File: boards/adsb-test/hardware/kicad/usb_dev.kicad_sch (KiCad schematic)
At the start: 0 parts

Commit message: Release v0.22.0: all ADSB_Test schematic sheets generated (ERC clean)
Co-Authored-By: Claude Opus 5.5 <noreply@anthropic.com>
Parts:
- added C1001, C1003, C1004, C1022, C1023: 1uF, Capacitor_SMD:C_0805_2012Metric_Pad1.18x1.45mm_HandSolder, symbol Device:C
- added C1002: 10uF, Capacitor_SMD:C_1206_3216Metric_Pad1.33x1.80mm_HandSolder, symbol Device:C
- added C1005, C1008, C1009, C1010, C1011, C1013, C1014, C1015, C1016, C1024, C1025, C1026, C1027, C1028, C1029, C1030, C1031, C1032, C1033, C1034, C1035, C1036, C1037: 100nF, Capacitor_SMD:C_0805_2012Metric_Pad1.18x1.45mm_HandSolder, symbol Device:C
- added C1006, C1007: 18pF, Capacitor_SMD:C_0805_2012Metric_Pad1.18x1.45mm_HandSolder, symbol Device:C
- added C1012, C1017: 4.7uF, Capacitor_SMD:C_0805_2012Metric_Pad1.18x1.45mm_HandSolder, symbol Device:C
- added C1018, C1019: 27pF, Capacitor_SMD:C_0805_2012Metric_Pad1.18x1.45mm_HandSolder, symbol Device:C
- added C1020, C1021: 15pF, Capacitor_SMD:C_0805_2012Metric_Pad1.18x1.45mm_HandSolder, symbol Device:C
- added D1001: 1N4148W, Diode_SMD:D_SOD-123, symbol Device:D
- added D1002: WS2812B, LED_SMD:LED_WS2812B_PLCC4_5.0x5.0mm_P3.2mm, symbol LED:WS2812B
- added J1001: Dev USB-C, Connector_USB:USB_C_Receptacle_GCT_USB4105-xx-A_16P_TopMnt_Horizontal, symbol Connector:USB_C_Receptacle_USB2.0_16P
- added Q1001, Q1002, Q1003, Q1004: MMBT3904, Package_TO_SOT_SMD:SOT-23_Handsoldering, symbol Transistor_BJT:MMBT3904
- added R1001, R1002: 5.1k, Resistor_SMD:R_0805_2012Metric_Pad1.20x1.40mm_HandSolder, symbol Device:R
- added R1003, R1004, R1005, R1006, R1007, R1008, R1010, R1015, R1017, R1018, R1019, R1020, R1021, R1022, R1023, R1024, R1025, R1033, R1034, R1039: 10k, Resistor_SMD:R_0805_2012Metric_Pad1.20x1.40mm_HandSolder, symbol Device:R
- added R1009, R1014: 12k 1%, Resistor_SMD:R_0805_2012Metric_Pad1.20x1.40mm_HandSolder, symbol Device:R
- added R1011, R1012, R1040: 100k, Resistor_SMD:R_0805_2012Metric_Pad1.20x1.40mm_HandSolder, symbol Device:R
- added R1013: 1M, Resistor_SMD:R_0805_2012Metric_Pad1.20x1.40mm_HandSolder, symbol Device:R
- added R1016: 2.2k, Resistor_SMD:R_0805_2012Metric_Pad1.20x1.40mm_HandSolder, symbol Device:R
- added R1030, R1031: 27R, Resistor_SMD:R_0805_2012Metric_Pad1.20x1.40mm_HandSolder, symbol Device:R
- added R1032, R1035: 1k, Resistor_SMD:R_0805_2012Metric_Pad1.20x1.40mm_HandSolder, symbol Device:R
- added R1036: 330R, Resistor_SMD:R_0805_2012Metric_Pad1.20x1.40mm_HandSolder, symbol Device:R
- added R1037, R1038: 0R, Resistor_SMD:R_0805_2012Metric_Pad1.20x1.40mm_HandSolder, symbol Device:R
- added SW1001: BOOTSEL (programmer), Button_Switch_THT:SW_PUSH_6mm, symbol Switch:SW_Push
- added TP1001: VBUS_DEV, TestPoint:TestPoint_Pad_D1.5mm, symbol Connector:TestPoint
- added TP1002: 3V3_DEV, TestPoint:TestPoint_Pad_D1.5mm, symbol Connector:TestPoint
- added TP1003: RP_SWCLK, TestPoint:TestPoint_Pad_D1.5mm, symbol Connector:TestPoint
- added TP1004: RP_SWDIO, TestPoint:TestPoint_Pad_D1.5mm, symbol Connector:TestPoint
- added TP1005: RP_RUN, TestPoint:TestPoint_Pad_D1.5mm, symbol Connector:TestPoint
- added TP1006: FT_A_DTR, TestPoint:TestPoint_Pad_D1.5mm, symbol Connector:TestPoint
- added TP1007: FT_A_RTS, TestPoint:TestPoint_Pad_D1.5mm, symbol Connector:TestPoint
- added TP1008: FT_B_DTR, TestPoint:TestPoint_Pad_D1.5mm, symbol Connector:TestPoint
- added TP1009: FT_B_RTS, TestPoint:TestPoint_Pad_D1.5mm, symbol Connector:TestPoint
- added U1001: USBLC6-2SC6, Package_TO_SOT_SMD:SOT-23-6_Handsoldering, symbol Power_Protection:USBLC6-2SC6
- added U1002: AP2112K-3.3, Package_TO_SOT_SMD:SOT-23-5_HandSoldering, symbol Regulator_Linear:AP2112K-3.3
- added U1003: USB2514B, ADSB_Test:QFN-36-1EP_6x6mm_P0.5mm_EP3.7x3.7mm_HandSolder, symbol Interface_USB:USB2514B_Bi
- added U1004: FT2232HL, Package_QFP:LQFP-64_10x10mm_P0.5mm, symbol Interface_USB:FT2232HL
- added U1005: 93LC56B, Package_SO:SOIC-8_3.9x4.9mm_P1.27mm, symbol Memory_EEPROM:93LCxxB
- added U1006, U1008: 74LVC1G07, Package_TO_SOT_SMD:SOT-23-5_HandSoldering, symbol 74xGxx:74LVC1G07
- added U1007, U1009, U1012, U1013, U1014, U1015: 74LVC1G125, Package_TO_SOT_SMD:SOT-23-5_HandSoldering, symbol 74xGxx:74LVC1G125
- added U1010: RP2040, ADSB_Test:QFN-56-1EP_7x7mm_P0.4mm_EP3.2x3.2mm_HandSolder, symbol MCU_RaspberryPi:RP2040
- added U1011: W25Q16JVSS, Package_SO:SOIC-8_5.3x5.3mm_P1.27mm, symbol Memory_Flash:W25Q16JVSS
- added Y1001: 24MHz, Crystal:Crystal_SMD_5032-2Pin_5.0x3.2mm_HandSoldering, symbol Device:Crystal
- added Y1002, Y1003: 12MHz, Crystal:Crystal_SMD_5032-2Pin_5.0x3.2mm_HandSoldering, symbol Device:Crystal
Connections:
- new net 3V3: R1020.1, R1021.1
- new net 3V3_DEV: C1002.1, C1008.1, C1009.1, C1010.1, C1011.1, C1012.1, C1015.1, C1016.1, C1022.1, C1024.1, C1025.1, C1026.1, C1028.1, C1030.1, C1031.1, C1032.1, C1033.1, C1034.1, C1035.1, C1036.1, C1037.1, R1003.1, R1004.1, R1010.1, R1015.1, R1017.1, R1018.1, R1019.1, R1033.1, R1034.1, R1039.1, TP1002.1, U1002.5 (VOUT), U1003.10 (VDDA33), U1003.15 (VDD33), U1003.23 (VDD33), U1003.29 (VDDA33), U1003.36 (VDDA33), U1003.5 (VDDA33), U1004.20 (VCCIO), U1004.31 (VCCIO), U1004.4 (VPHY), U1004.42 (VCCIO), U1004.50 (VREGIN), U1004.56 (VCCIO), U1004.9 (VPLL), U1005.8 (VCC), U1006.5 (VCC), U1007.5 (VCC), U1008.5 (VCC), U1009.5 (VCC), U1010.1 (IOVDD), U1010.10 (IOVDD), U1010.22 (IOVDD), U1010.33 (IOVDD), U1010.42 (IOVDD), U1010.43 (ADC_AVDD), U1010.44 (VREG_VIN), U1010.48 (USB_VDD), U1010.49 (IOVDD), U1011.8 (VCC), U1012.5 (VCC), U1013.5 (VCC), U1014.5 (VCC), U1015.5 (VCC)
- new net C5_BOOT: Q1004.3 (C)
- new net C5_CON_RX: R1021.2, U1008.4
- new net C5_CON_TX: U1009.2
- new net C5_EN: Q1003.3 (C)
- new net DEV_CC1: J1001.A5 (CC1), R1001.1
- new net DEV_CC2: J1001.B5 (CC2), R1002.1
- new net DEV_DM: J1001.A7 (D-), J1001.B7 (D-), U1001.3 (I/O2), U1001.4 (I/O2), U1003.30 (USBDM_UP)
- new net DEV_DP: J1001.A6 (D+), J1001.B6 (D+), U1001.1 (I/O1), U1001.6 (I/O1), U1003.31 (USBDP_UP)
- new net DEV_M1421_NRST: U1012.4
- new net DEV_M1421_SYNC: U1013.4
- new net DEV_M1421_TX: U1014.4
- new net ETH_TXD1_BOOT: Q1002.3 (C)
- new net FT_1V8: C1013.1, C1014.1, C1017.1, U1004.12 (VCORE), U1004.37 (VCORE), U1004.49 (VREGOUT), U1004.64 (VCORE)
- new net FT_A_DTR: Q1002.2 (E), R1022.1, TP1006.1, U1004.21 (ADBUS4)
- new net FT_A_RTS: Q1001.2 (E), R1023.1, TP1007.1, U1004.18 (ADBUS2)
- new net FT_A_RXD: U1004.17 (ADBUS1), U1007.4
- new net FT_A_TXD: U1004.16 (ADBUS0), U1006.2
- new net FT_B_DTR: Q1004.2 (E), R1024.1, TP1008.1, U1004.43 (BDBUS4)
- new net FT_B_RTS: Q1003.2 (E), R1025.1, TP1009.1, U1004.40 (BDBUS2)
- new net FT_B_RXD: U1004.39 (BDBUS1), U1009.4
- new net FT_B_TXD: U1004.38 (BDBUS0), U1008.2
- new net FT_DM: U1003.6 (USBDM_DN3/PRT_DIS_M3), U1004.7 (DM)
- new net FT_DP: U1003.7 (USBDP_DN3/PRT_DIS_P3), U1004.8 (DP)
- new net FT_EECLK: R1018.2, U1004.62 (EECLK), U1005.2 (SCLK)
- new net FT_EECS: R1017.2, U1004.63 (EECS), U1005.1 (CS)
- new net FT_EEDATA: R1016.2, R1019.2, U1004.61 (EEDATA), U1005.3 (DI)
- new net FT_EEDO: R1016.1, U1005.4 (DO)
- new net FT_REF: R1014.1, U1004.6 (REF)
- new net FT_RESET: R1015.2, U1004.14 (~{RESET})
- new net FT_XI: C1018.1, U1004.2 (OSCI), Y1002.1
- new net FT_XO: C1019.1, U1004.3 (OSCO), Y1002.2
- new net GND: C1001.2, C1002.2, C1003.2, C1004.2, C1005.2, C1006.2, C1007.2, C1008.2, C1009.2, C1010.2, C1011.2, C1012.2, C1013.2, C1014.2, C1015.2, C1016.2, C1017.2, C1018.2, C1019.2, C1020.2, C1021.2, C1022.2, C1023.2, C1024.2, C1025.2, C1026.2, C1027.2, C1028.2, C1029.2, C1030.2, C1031.2, C1032.2, C1033.2, C1034.2, C1035.2, C1036.2, C1037.2, D1002.3 (VSS), J1001.A1 (GND), J1001.A12 (GND), J1001.B1 (GND), J1001.B12 (GND), J1001.SH (SHIELD), R1001.2, R1002.2, R1005.2, R1006.2, R1007.2, R1008.2, R1009.2, R1012.2, R1014.2, R1040.2, SW1001.2, U1001.2 (GND), U1002.2 (GND), U1003.11 (TEST), U1003.37 (VSS), U1004.1 (GND), U1004.10 (AGND), U1004.11 (GND), U1004.13 (TEST), U1004.15 (GND), U1004.25 (GND), U1004.35 (GND), U1004.47 (GND), U1004.5 (GND), U1004.51 (GND), U1005.5 (GND), U1006.3 (GND), U1007.1, U1007.3 (GND), U1008.3 (GND), U1009.1, U1009.3 (GND), U1010.19 (TESTEN), U1010.57 (GND), U1011.4 (GND), U1012.1, U1012.3 (GND), U1013.1, U1013.3 (GND), U1014.1, U1014.3 (GND), U1015.1, U1015.3 (GND)
- new net HUB_CFG0: R1005.1, U1003.24 (SCL/SMBCLK/CFG_SEL0)
- new net HUB_CFG1: R1006.1, U1003.25 (HS_IND/CFG_SEL1)
- new net HUB_CRFILT: C1003.1, U1003.14 (CRFILT)
- new net HUB_DN2_M: R1004.2, U1003.3 (USBDM_DN2/PRT_DIS_M2)
- new net HUB_DN2_P: R1003.2, U1003.4 (USBDP_DN2/PRT_DIS_P2)
- new net HUB_NONREM0: R1007.1, U1003.28 (SUSP_IND/LOCAL_PWR/NON_REM0)
- new net HUB_NONREM1: R1008.1, U1003.22 (SDA/SMBDATA/NON_REM1)
- new net HUB_PLLFILT: C1004.1, U1003.34 (PLLFILT)
- new net HUB_RBIAS: R1009.1, U1003.35 (RBIAS)
- new net HUB_RESET: C1005.1, R1010.2, U1003.26 (RESET_N)
- new net HUB_VBUS_DET: R1011.2, R1012.1, U1003.27 (VBUS_DET)
- new net HUB_XI: C1006.1, R1013.1, U1003.33 (XTALIN/CLKIN), Y1001.1
- new net HUB_XO: C1007.1, R1013.2, U1003.32 (XTALOUT), Y1001.2
- new net LED_VDD: C1029.1, D1001.1 (K), D1002.1 (VDD)
- new net M1421_SUTX: U1015.2
- new net P4_CON_RX: R1020.2, U1006.4
- new net P4_CON_TX: U1007.2
- new net P4_EN: Q1001.3 (C)
- new net P4_USJ_DM: U1003.1 (USBDM_DN1/PRT_DIS_M1)
- new net P4_USJ_DP: U1003.2 (USBDP_DN1/PRT_DIS_P1)
- new net QA1_B: Q1001.1 (B), R1022.2
- new net QA2_B: Q1002.1 (B), R1023.2
- new net QB1_B: Q1003.1 (B), R1024.2
- new net QB2_B: Q1004.1 (B), R1025.2
- new net RP_1V1: C1023.1, C1027.1, U1010.23 (DVDD), U1010.45 (VREG_VOUT), U1010.50 (DVDD)
- new net RP_BOOTSEL: R1035.2, SW1001.1
- new net RP_DM: R1031.2, U1010.46 (USB_DM)
- new net RP_DM_H: R1031.1, U1003.8 (USBDM_DN4/PRT_DIS_M4)
- new net RP_DP: R1030.2, U1010.47 (USB_DP)
- new net RP_DP_H: R1030.1, U1003.9 (USBDP_DN4/PRT_DIS_P4)
- new net RP_LED: R1036.1, U1010.27 (GPIO16)
- new net RP_LED_D: D1002.4 (DIN), R1036.2
- new net RP_NRST: R1037.1, U1010.38 (GPIO26/ADC0)
- new net RP_NRST_L: R1037.2, R1039.2, U1012.2
- new net RP_QD0: U1010.53 (QSPI_SD0), U1011.5 (DI/IO_{0})
- new net RP_QD1: U1010.55 (QSPI_SD1), U1011.2 (DO/IO_{1})
- new net RP_QD2: U1010.54 (QSPI_SD2), U1011.3 (~{WP}/IO_{2})
- new net RP_QD3: U1010.51 (QSPI_SD3), U1011.7 (~{HOLD}/~{RESET}/IO_{3})
- new net RP_QSCK: U1010.52 (QSPI_SCLK), U1011.6 (CLK)
- new net RP_QSS: R1034.2, R1035.1, U1010.56 (~{QSPI_SS}), U1011.1 (~{CS})
- new net RP_RUN: R1033.2, TP1005.1, U1010.26 (RUN)
- new net RP_RX: U1010.41 (GPIO29/ADC3), U1015.4
- new net RP_SWCLK: TP1003.1, U1010.24 (SWCLK)
- new net RP_SWDIO: TP1004.1, U1010.25 (SWDIO)
- new net RP_SYNC: R1038.1, U1010.39 (GPIO27/ADC1)
- new net RP_SYNC_L: R1038.2, R1040.1, U1013.2
- new net RP_TX: U1010.40 (GPIO28/ADC2), U1014.2
- new net RP_XI: C1020.1, U1010.20 (XIN), Y1003.1
- new net RP_XO: R1032.2, U1010.21 (XOUT)
- new net RP_XO_R: C1021.1, R1032.1, Y1003.2
- new net VBUS_DEV: C1001.1, D1001.2 (A), J1001.A4 (VBUS), J1001.A9 (VBUS), J1001.B4 (VBUS), J1001.B9 (VBUS), R1011.1, TP1001.1, U1001.5 (VBUS), U1002.1 (VIN), U1002.3 (EN)
- no-connect marks 0 -> 66
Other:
- note added: "DEV PORT (own 3V3_DEV domain from Dev VBUS; works with the target unpowered): USB-C -> USBLC6 -> USB2514B hub (strap defaults, bus powered). DN1 P4 USB-Serial/JTAG, DN2 disabled (C5 USB = SDIO pins), DN3 FT2232HL: A = P4 UART0, B = C5 UART0, DTR/RTS -> MMBT3904 pairs (esptool auto-reset) on P4_EN/BOOT and C5_EN/BOOT. DN4 RP2040 + W25Q16 running the STOCK ADSBee 1421 Programmer: GPIO26 ~SRST, 27 S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"

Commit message: Release v0.23.0: ADSB_Test BOM with DigiKey/LCSC codes and order links; 27 pF crystal load caps
Co-Authored-By: Claude Opus 5.5 <noreply@anthropic.com>
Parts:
- C1006, C1007: value 18pF -> 27pF
- C1020, C1021: value 15pF -> 27pF

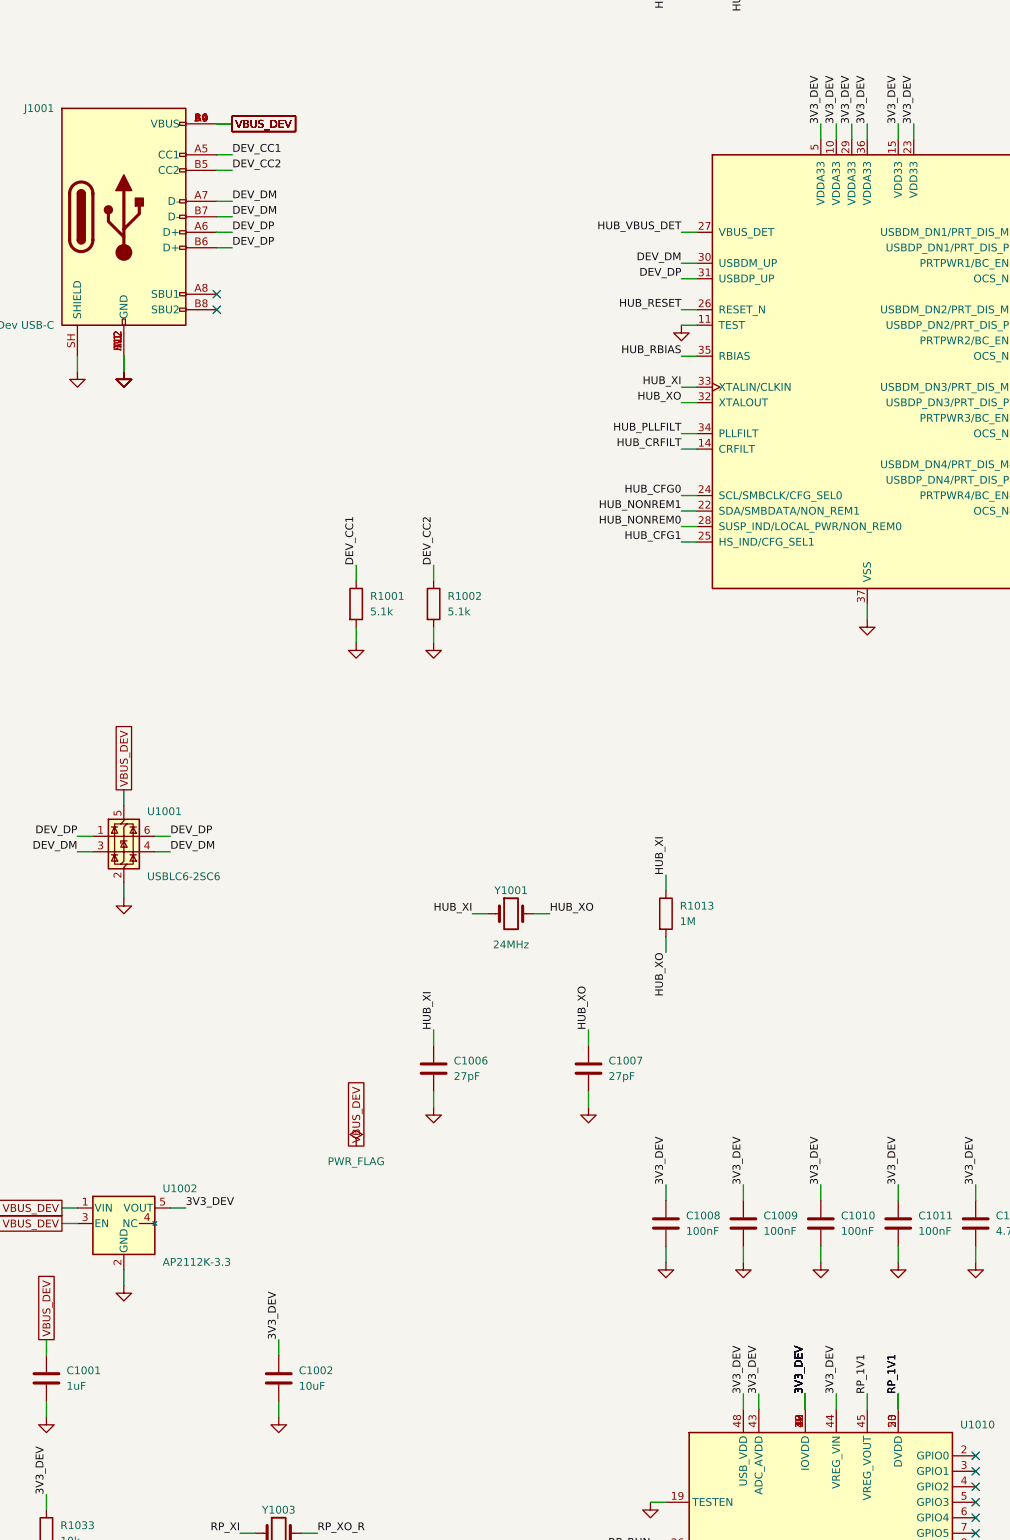
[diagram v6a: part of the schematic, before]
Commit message: Schematic generator: hide stacked pins (KiCad convention) so pin numbers don't overprint
Co-Authored-By: Claude Opus 5.5 <noreply@anthropic.com>
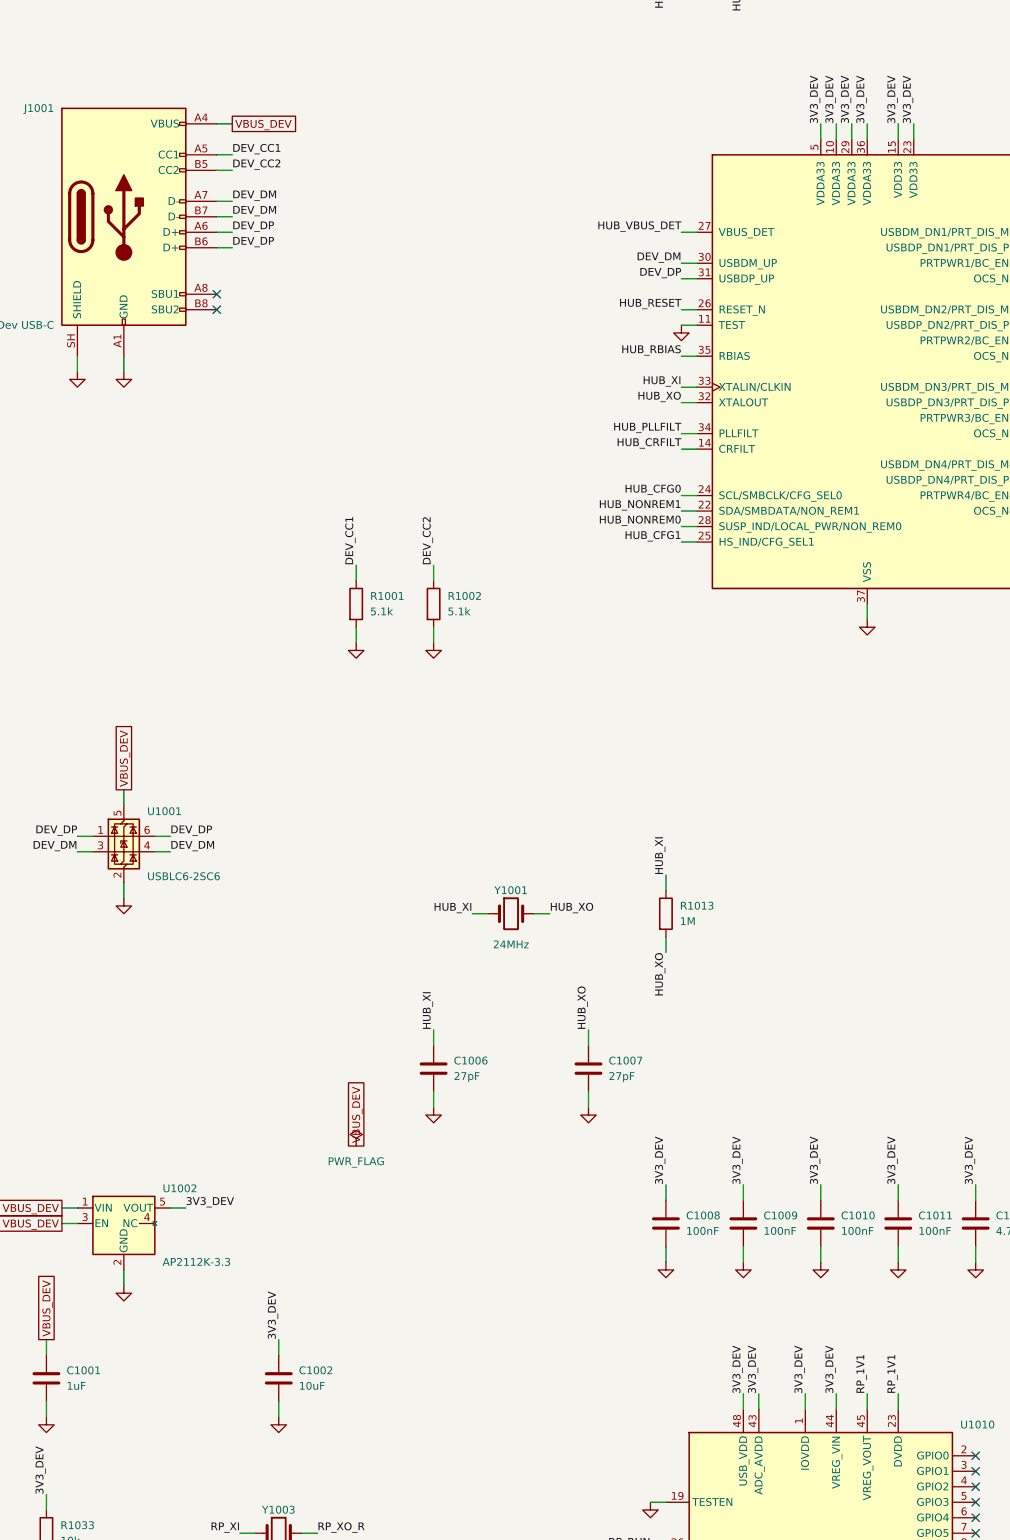
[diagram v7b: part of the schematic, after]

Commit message: ADSB_Test: net classes + diff-pair rules, USB pairs renamed _D_P/_D_N, U201 VSYS drawn at the bottom
Co-Authored-By: Claude Opus 5.5 <noreply@anthropic.com>
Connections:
- net DEV_DM renamed DEV_D_N
- net DEV_DP renamed DEV_D_P
- net FT_DM renamed FT_D_N
- net FT_DP renamed FT_D_P
- net P4_USJ_DM renamed P4_USJ_D_N
- net P4_USJ_DP renamed P4_USJ_D_P
- net RP_DM renamed RP_D_N
- net RP_DM_H renamed RP_HUB_D_N
- net RP_DP renamed RP_D_P
- net RP_DP_H renamed RP_HUB_D_P
